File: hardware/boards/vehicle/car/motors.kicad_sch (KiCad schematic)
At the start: 42 parts, among them M1 Motor_DC, M2 Motor_DC, Q1 FQP27P06, Q10 AO3400A, Q11 2N3904, Q12 2N3904, Q2 AO3400A, Q3 FQP27P06, Q4 AO3400A, Q5 2N3904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

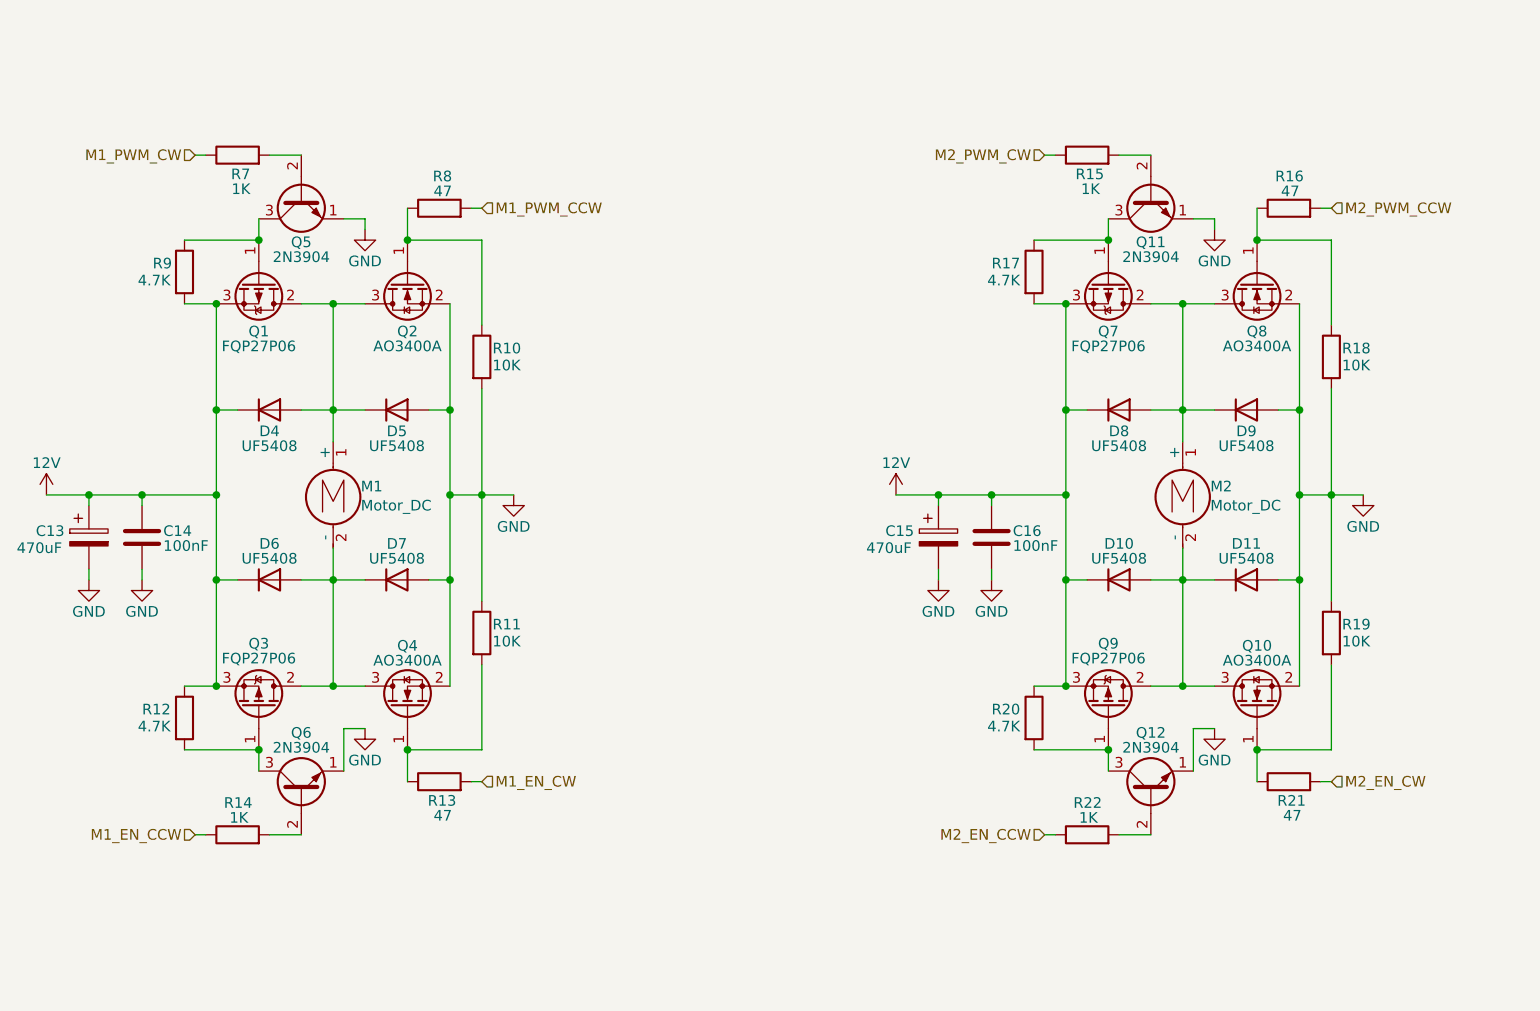
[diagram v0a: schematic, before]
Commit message: added all footprints for lidar and car
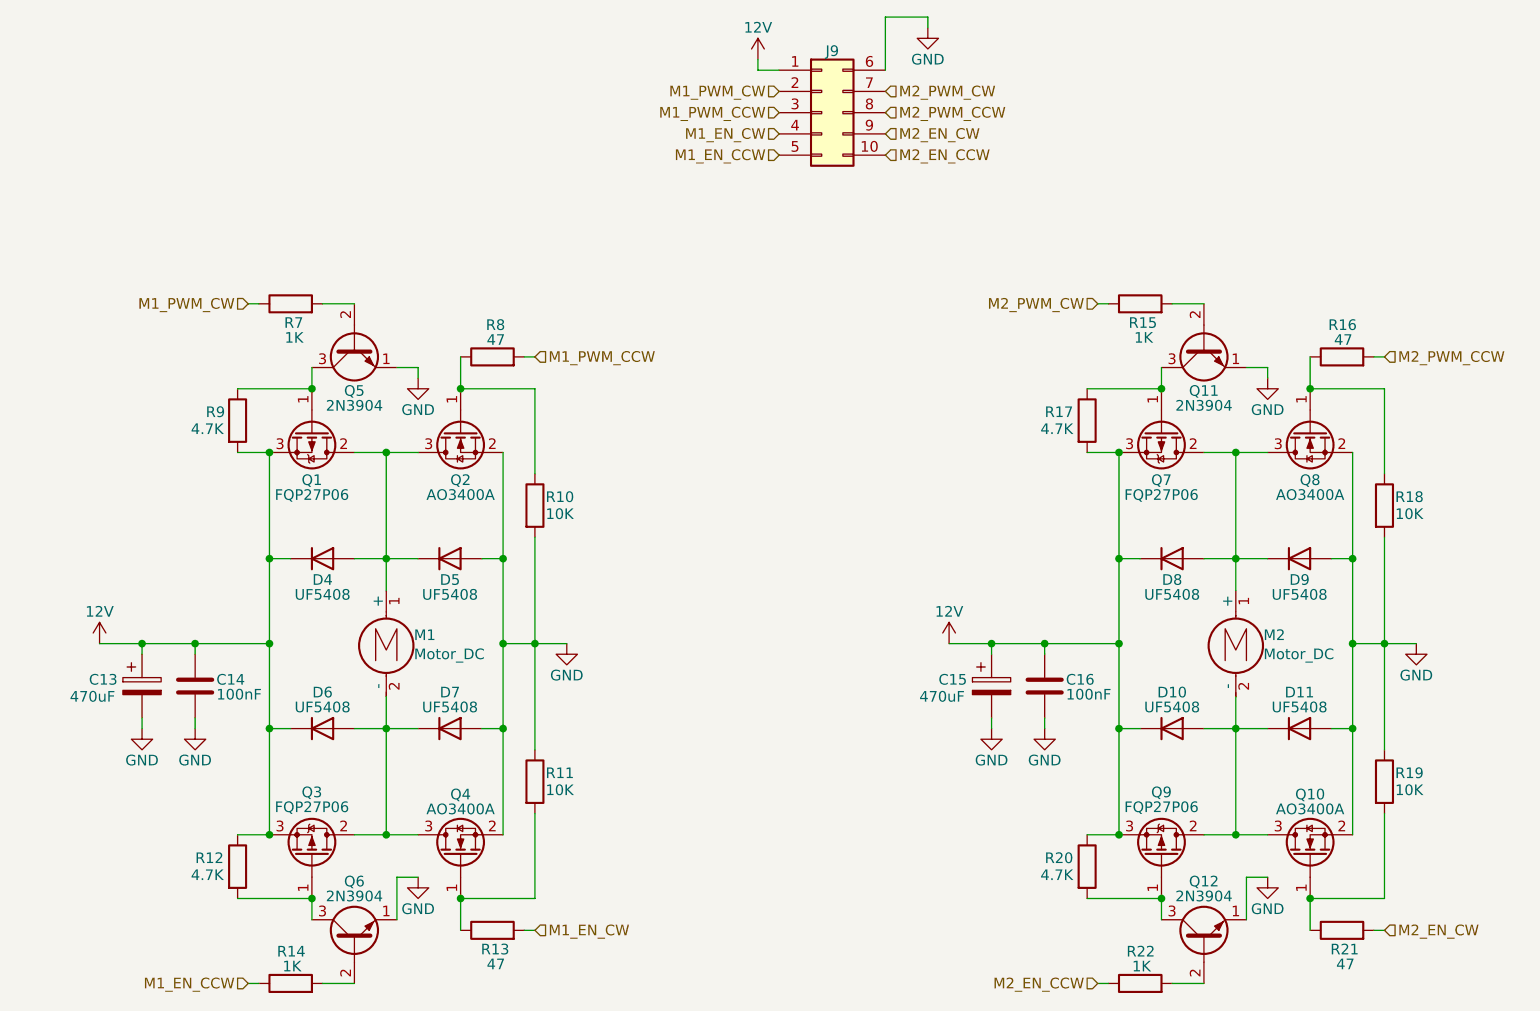
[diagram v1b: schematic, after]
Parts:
- added J9: Conn_02x05_Top_Bottom, Connector_PinHeader_2.54mm:PinHeader_2x05_P2.54mm_Vertical, symbol Connector_Generic:Conn_02x05_Top_Bottom
- C13, C15: footprint (none) -> Capacitor_THT:CP_Radial_D10.0mm_P5.00mm
- C14, C16: footprint (none) -> Capacitor_SMD:C_0603_1608Metric_Pad1.08x0.95mm_HandSolder
- M1, M2: footprint (none) -> Connector_PinHeader_2.54mm:PinHeader_1x02_P2.54mm_Vertical
- R10, R11, R12, R13, R14, R15, R16, R17, R18, R19, R20, R21, R22, R7, R8, R9: footprint (none) -> Resistor_SMD:R_0603_1608Metric_Pad0.98x0.95mm_HandSolder
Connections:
- net 12V: now also J9.1 (Pin_1)
- net GND: now also J9.6 (Pin_6)
- net M1_EN_CCW: now also J9.5 (Pin_5)
- net M1_EN_CW: now also J9.4 (Pin_4)
- net M1_PWM_CCW: now also J9.3 (Pin_3)
- net M1_PWM_CW: now also J9.2 (Pin_2)
- net M2_EN_CCW: now also J9.10 (Pin_10)
- net M2_EN_CW: now also J9.9 (Pin_9)
- net M2_PWM_CCW: now also J9.8 (Pin_8)
- net M2_PWM_CW: now also J9.7 (Pin_7)
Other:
- moved on the sheet: C13, C14, C15, C16, D10, D11, D4, D5, D6, D7, D8, D9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

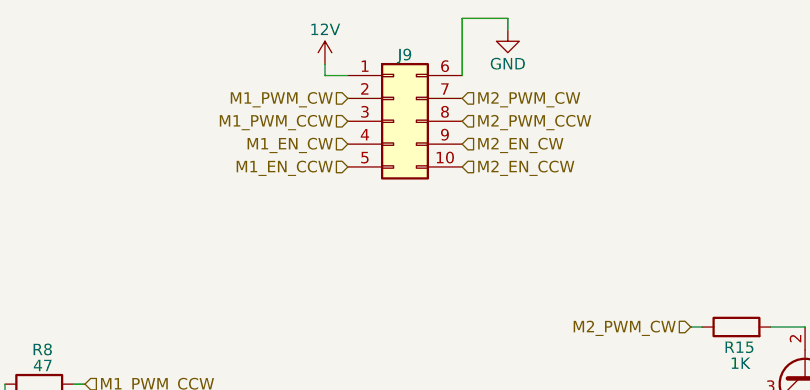
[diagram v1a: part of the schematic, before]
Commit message: corrected SD card and transceiver on symbol and schema
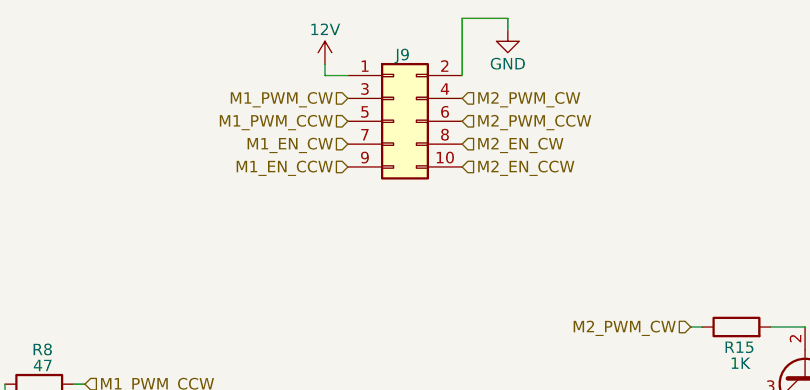
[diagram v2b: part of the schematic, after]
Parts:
- removed J9: Conn_02x05_Top_Bottom, Connector_PinHeader_2.54mm:PinHeader_2x05_P2.54mm_Vertical, symbol Connector_Generic:Conn_02x05_Top_Bottom
- added J9: Conn_02x05_Odd_Even, Connector_PinHeader_2.54mm:PinHeader_2x05_P2.54mm_Vertical, symbol Connector_Generic:Conn_02x05_Odd_Even
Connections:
- net 12V: now also J9.1 (Pin_1)
- net GND: now also J9.2 (Pin_2)
- net M1_EN_CCW: now also J9.9 (Pin_9)
- net M1_EN_CW: now also J9.7 (Pin_7)
- net M1_PWM_CCW: now also J9.5 (Pin_5)
- net M1_PWM_CW: now also J9.3 (Pin_3)
- net M2_EN_CCW: now also J9.10 (Pin_10)
- net M2_EN_CW: now also J9.8 (Pin_8)
- net M2_PWM_CCW: now also J9.6 (Pin_6)
- net M2_PWM_CW: now also J9.4 (Pin_4)
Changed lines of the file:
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@@
 	(wire
 		(pts
+			(xy 160.02 33.02) (xy 160.02 34.29)
+		)
+		(stroke
+			(width 0)
+			(type default)
+		)
+	)
+	(wire
+		(pts
 			(xy 205.74 138.43) (xy 214.63 138.43)
 		)
@@
 	(wire
 		(pts
-			(xy 109.22 85.09) (xy 109.22 97.79)
+			(xy 154.94 39.37) (xy 154.94 33.02)
 		)
 		(stroke
@@
 	(wire
 		(pts
-			(xy 106.68 118.11) (xy 109.22 118.11)
+			(xy 109.22 85.09) (xy 109.22 97.79)
 		)
 		(stroke
@@
 	(wire
 		(pts
-			(xy 113.03 95.25) (xy 113.03 107.95)
+			(xy 106.68 118.11) (xy 109.22 118.11)
 		)
 		(stroke
@@
 	(wire
 		(pts
-			(xy 196.85 97.79) (xy 196.85 101.6)
+			(xy 113.03 95.25) (xy 113.03 107.95)
 		)
 		(stroke
@@
 	(wire
 		(pts
-			(xy 77.47 85.09) (xy 81.28 85.09)
+			(xy 196.85 97.79) (xy 196.85 101.6)
 		)
 		(stroke
@@
 	(wire
 		(pts
-			(xy 182.88 118.11) (xy 182.88 130.81)
+			(xy 77.47 85.09) (xy 81.28 85.09)
 		)
 		(stroke
@@
 	(wire
 		(pts
-			(xy 139.7 39.37) (xy 139.7 38.1)
+			(xy 182.88 118.11) (xy 182.88 130.81)
 		)
 		(stroke
@@
 	(wire
 		(pts
-			(xy 154.94 33.02) (xy 160.02 33.02)
-		)
-		(stroke
-			(width 0)
-			(type default)
-		)
-	)
-	(wire
-		(pts
 			(xy 187.96 138.43) (xy 187.96 140.97)
 		)
@@
 	(wire
 		(pts
+			(xy 154.94 33.02) (xy 160.02 33.02)
+		)
+		(stroke
+			(width 0)
+			(type default)
+		)
+	)
+	(wire
+		(pts
 			(xy 198.12 140.97) (xy 198.12 135.89)
 		)
@@
 	(wire
 		(pts
-			(xy 106.68 97.79) (xy 109.22 97.79)
+			(xy 142.24 39.37) (xy 139.7 39.37)
 		)
 		(stroke
@@
 	(wire
 		(pts
-			(xy 96.52 135.89) (xy 99.06 135.89)
+			(xy 106.68 97.79) (xy 109.22 97.79)
 		)
 		(stroke
@@
 	(wire
 		(pts
-			(xy 180.34 148.59) (xy 181.61 148.59)
+			(xy 96.52 135.89) (xy 99.06 135.89)
 		)
 		(stroke
@@
 	(wire
 		(pts
-			(xy 167.64 107.95) (xy 173.99 107.95)
+			(xy 180.34 148.59) (xy 181.61 148.59)
 		)
 		(stroke
@@
 	(wire
 		(pts
-			(xy 214.63 107.95) (xy 214.63 120.65)
+			(xy 167.64 107.95) (xy 173.99 107.95)
 		)
 		(stroke
@@
 	(wire
 		(pts
-			(xy 154.94 39.37) (xy 154.94 33.02)
+			(xy 214.63 107.95) (xy 214.63 120.65)
 		)
 		(stroke
@@
 	(wire
 		(pts
-			(xy 160.02 33.02) (xy 160.02 34.29)
-		)
-		(stroke
-			(width 0)
-			(type default)
-		)
-	)
-	(wire
-		(pts
-			(xy 142.24 39.37) (xy 139.7 39.37)
-		)
-		(stroke
-			(width 0)
-			(type default)
-		)
-	)
-	(wire
-		(pts
 			(xy 91.44 130.81) (xy 95.25 130.81)
 		)
@@
 	(wire
 		(pts
+			(xy 139.7 39.37) (xy 139.7 38.1)
+		)
+		(stroke
+			(width 0)
+			(type default)
+		)
+	)
+	(wire
+		(pts
 			(xy 193.04 85.09) (xy 196.85 85.09)
 		)
@@
 		)
 	)
-	(hierarchical_label "M1_PWM_CCW"
+	(hierarchical_label "M2_PWM_CCW"
 		(shape input)
-		(at 142.24 44.45 180)
+		(at 154.94 44.45 0)
 		(effects
 			(font
 				(size 1.27 1.27)
 			)
-			(justify right)
+			(justify left)
+		)
+	)
+	(hierarchical_label "M2_PWM_CW"
+		(shape input)
+		(at 154.94 41.91 0)
+		(effects
+			(font
+				(size 1.27 1.27)
+			)
+			(justify left)
 		)
 	)
@@
 		)
 	)
-	(hierarchical_label "M2_EN_CCW"
+	(hierarchical_label "M1_EN_CCW"
 		(shape input)
-		(at 154.94 49.53 0)
+		(at 142.24 49.53 180)
 		(effects
 			(font
 				(size 1.27 1.27)
 			)
-			(justify left)
+			(justify right)
 		)
 	)
-	(hierarchical_label "M2_PWM_CW"
+	(hierarchical_label "M1_PWM_CW"
 		(shape input)
-		(at 154.94 41.91 0)
+		(at 142.24 41.91 180)
 		(effects
 			(font
 				(size 1.27 1.27)
 			)
-			(justify left)
+			(justify right)
 		)
 	)
-	(hierarchical_label "M1_EN_CCW"
+	(hierarchical_label "M1_PWM_CCW"
 		(shape input)
-		(at 142.24 49.53 180)
+		(at 142.24 44.45 180)
 		(effects
 			(font
@@
 		)
 	)
-	(hierarchical_label "M1_PWM_CW"
+	(hierarchical_label "M2_EN_CCW"
 		(shape input)
-		(at 142.24 41.91 180)
+		(at 154.94 49.53 0)
 		(effects
 			(font
 				(size 1.27 1.27)
 			)
-			(justify right)
+			(justify left)
 		)
 	)
@@
 		)
 	)
-	(hierarchical_label "M2_PWM_CCW"
-		(shape input)
-		(at 154.94 44.45 0)
-		(effects
-			(font
-				(size 1.27 1.27)
-			)
-			(justify left)
-		)
-	)
 	(symbol
 		(lib_id "power:GND")
@@
 	)
 	(symbol
-		(lib_id "Connector_Generic:Conn_02x05_Top_Bottom")
-		(at 147.32 44.45 0)
-		(unit 1)
-		(exclude_from_sim no)
-		(in_bom yes)
-		(on_board yes)
-		(dnp no)
-		(property "Reference" "J9"
-			(at 148.59 37.084 0)
-			(effects
-				(font
-					(size 1.27 1.27)
-				)
-			)
-		)
-		(property "Value" "Conn_02x05_Top_Bottom"
-			(at 148.59 35.56 0)
-			(effects
-				(font
-					(size 1.27 1.27)
-				)
-				(hide yes)
-			)
-		)
-		(property "Footprint" "Connector_PinHeader_2.54mm:PinHeader_2x05_P2.54mm_Vertical"
-			(at 147.32 44.45 0)
-			(effects
-				(font
-					(size 1.27 1.27)
-				)
-				(hide yes)
-			)
-		)
-		(property "Datasheet" "~"
-			(at 147.32 44.45 0)
-			(effects
-				(font
-					(size 1.27 1.27)
-				)
-				(hide yes)
-			)
-		)
-		(property "Description" "Generic connector, double row, 02x05, top/bottom pin numbering scheme (row 1: 1...pins_per_row, row2: pins_per_row+1 ... num_pins), script generated (kicad-library-utils/schlib/autogen/connector/)"
-			(at 147.32 44.45 0)
-			(effects
-				(font
-					(size 1.27 1.27)
-				)
-				(hide yes)
-			)
-		)
-		(pin "3"
-		)
-		(pin "1"
-		)
-		(pin "2"
-		)
-		(pin "7"
-		)
-		(pin "10"
-		)
-		(pin "9"
-		)
-		(pin "8"
-		)
-		(pin "5"
-		)
-		(pin "4"
-		)
-		(pin "6"
-		)
-		(instances
-			(project ""
-				(path "/d4bcaa97-404f-4040-88d9-84162ce8c00c/3a79dc46-7c20-4cbf-828b-ee9f07ae0d45"
-					(reference "J9")
-					(unit 1)
-				)
-			)
-		)
-	)
-	(symbol
 		(lib_id "Diode:UF5408")
 		(at 189.23 97.79 0)
@@
 					(unit 1)
 				)
+			)
+		)
+	)
+	(symbol
+		(lib_id "Connector_Generic:Conn_02x05_Odd_Even")
+		(at 147.32 44.45 0)
+		(unit 1)
+		(exclude_from_sim no)
+		(in_bom yes)
+		(on_board yes)
+		(dnp no)
+		(property "Reference" "J9"
+			(at 148.336 37.084 0)
+			(effects
+				(font
+					(size 1.27 1.27)
+				)
+			)
+		)
+		(property "Value" "Conn_02x05_Odd_Even"
+			(at 148.59 35.56 0)
+			(effects
+				(font
+					(size 1.27 1.27)
+				)
+				(hide yes)
+			)
+		)
+		(property "Footprint" "Connector_PinHeader_2.54mm:PinHeader_2x05_P2.54mm_Vertical"
+			(at 147.32 44.45 0)
+			(effects
+				(font
+					(size 1.27 1.27)
+				)
+				(hide yes)
+			)
+		)
+		(property "Datasheet" "~"
+			(at 147.32 44.45 0)
+			(effects
+				(font
+					(size 1.27 1.27)
+				)
+				(hide yes)
+			)
+		)
+		(property "Description" "Generic connector, double row, 02x05, odd/even pin numbering scheme (row 1 odd numbers, row 2 even numbers), script generated (kicad-library-utils/schlib/autogen/connector/)"
+			(at 147.32 44.45 0)
+			(effects
+				(font
+					(size 1.27 1.27)
+				)
+				(hide yes)
+			)
+		)
+		(pin "7"
+		)
+		(pin "2"
+		)
+		(pin "6"
+		)
+		(pin "3"
+		)
+		(pin "1"
+		)
+		(pin "5"
+		)
+		(pin "9"
+		)
+		(pin "4"
+		)
+		(pin "8"
+		)
+		(pin "10"
+		)
+		(instances
+			(project ""
+				(path "/d4bcaa97-404f-4040-88d9-84162ce8c00c/3a79dc46-7c20-4cbf-828b-ee9f07ae0d45"
+					(reference "J9")
+					(unit 1)
+				)

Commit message: pcb for car
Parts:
- D10, D11, D4, D5, D6, D7, D8, D9: value UF5408 -> SS36; footprint Diode_THT:D_DO-201AD_P15.24mm_Horizontal -> Diode_SMD:D_SMA_Handsoldering
